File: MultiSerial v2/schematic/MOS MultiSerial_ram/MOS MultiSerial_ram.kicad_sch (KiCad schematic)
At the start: 34 parts, among them J10 ., J11 ., J12 Conn_01x01, J13 Conn_01x04, J14 Conn_01x02, J6 Conn_01x04, J7 Conn_02x04_Odd_Even, J8 ., J9 Conn_01x01, U1 6551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

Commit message: python work
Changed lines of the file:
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@@
     (effects (font (size 1.27 1.27)) (justify left bottom))
   )
-  (label "TX2" (at 14.605 46.355 0) (fields_autoplaced)
+  (label "TX2" (at 14.605 43.815 0) (fields_autoplaced)
     (effects (font (size 1.27 1.27)) (justify left bottom))
   )
@@
     (effects (font (size 1.27 1.27)) (justify right bottom))
   )
-  (label "TX3" (at 14.605 51.435 0) (fields_autoplaced)
+  (label "TX3" (at 14.605 48.895 0) (fields_autoplaced)
     (effects (font (size 1.27 1.27)) (justify left bottom))
   )
@@
     (effects (font (size 1.27 1.27)) (justify left bottom))
   )
-  (label "RX3" (at 14.605 48.895 0) (fields_autoplaced)
+  (label "RX3" (at 14.605 51.435 0) (fields_autoplaced)
     (effects (font (size 1.27 1.27)) (justify left bottom))
   )
@@
     (effects (font (size 1.27 1.27)) (justify left bottom))
   )
-  (label "RX2" (at 14.605 43.815 0) (fields_autoplaced)
-    (effects (font (size 1.27 1.27)) (justify left bottom))
-  )
+  (label "RX2" (at 14.605 46.355 0) (fields_autoplaced)
+    (effects (font (size 1.27 1.27)) (justify left bottom))
+  )

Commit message: python work
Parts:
- added J24: Conn_01x01, Connector_PinHeader_2.00mm:PinHeader_1x01_P2.00mm_Vertical, symbol Connector_Generic:Conn_01x01
- added U10: 74AHC1G08, Package_TO_SOT_SMD:SOT-23-5_HandSoldering, symbol 74xGxx:74AHC1G08
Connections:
- net +3V3: now also U10.5 (VCC)
- net GND: now also U10.3 (GND)
- net ~{CS_ACIA2}: now also J24.1 (Pin_1), U10.2
- net ~{CS_ACIA}: now also U10.1
- new net Bus/~{DOE}: U10.4
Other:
- moved on the sheet: C5, J10, J11, J12, J14, J8, J9, JP4, JP5, R1, R2, R3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

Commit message: Documentation update
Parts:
- added U11: 74AHC1G14, Package_TO_SOT_SMD:SOT-23-5, symbol 74xGxx:74AHC1G14
- added U12: 74AHC1G32, symbol 74xGxx:74AHC1G32
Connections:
- net +3V3: now also U11.5 (VCC), U12.5 (VCC)
- net Bus/~{DOE}: now also U12.4; no longer U10.4
- net GND: now also U11.3 (GND), U12.3 (GND)
- net ~{RST}: now also U11.2
- new net: U10.4, U12.1
- new net: U11.4, U12.2
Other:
- note added: "Low if CS is low and ~{RST} is high."
- note added: "Low if one or the other is low."
- moved on the sheet: J10, J11, J12, J14, J6, J7, J9, JP1, JP2, JP3, JP4, JP5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

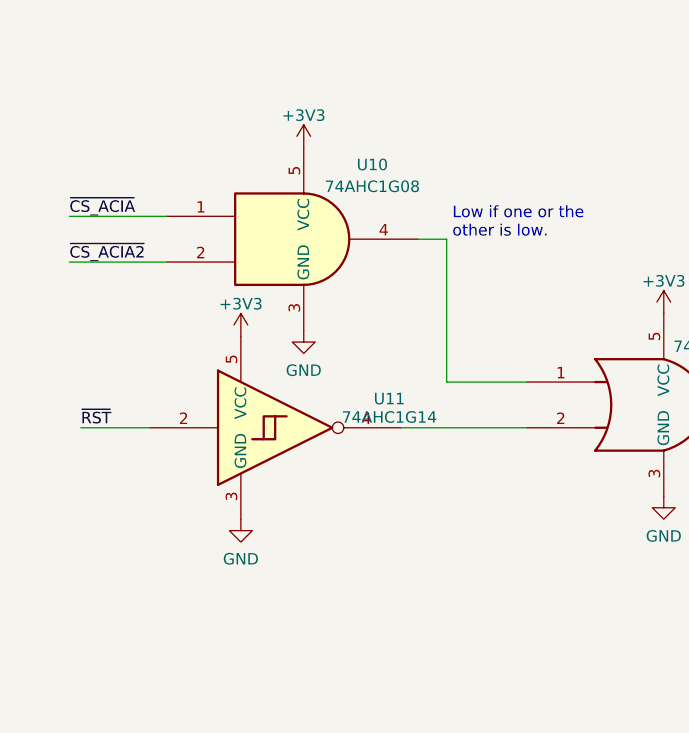
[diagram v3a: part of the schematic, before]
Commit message: Documentation update, 6800 working, new computers added
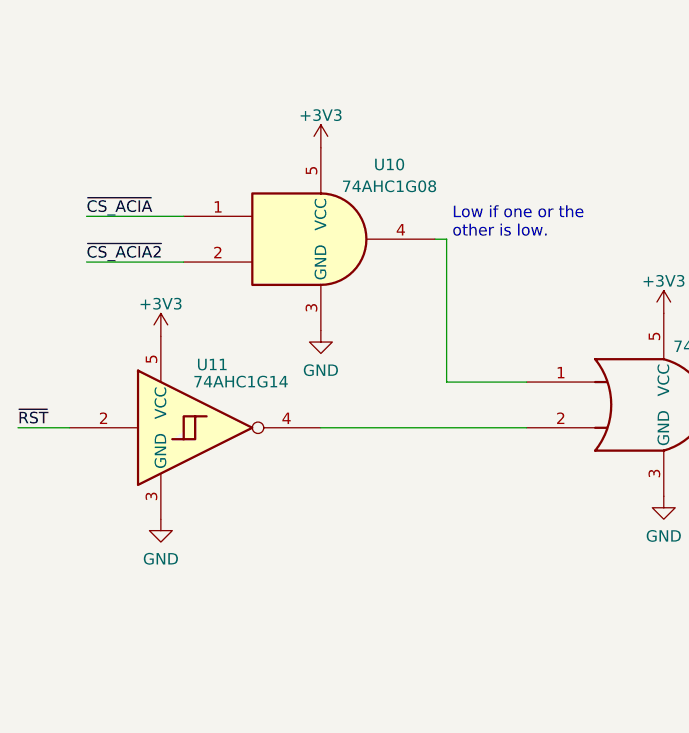
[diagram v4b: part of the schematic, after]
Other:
- moved on the sheet: U10, U11
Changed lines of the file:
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@@
     (stroke (width 0) (type default))
   )
-  (wire (pts (xy 60.96 41.91) (xy 57.785 41.91))
+  (wire (pts (xy 60.96 41.91) (xy 59.69 41.91))
     (stroke (width 0) (type default))
   )
@@
     (stroke (width 0) (type default))
   )
-  (wire (pts (xy 19.05 39.37) (xy 29.845 39.37))
+  (wire (pts (xy 20.955 39.37) (xy 31.75 39.37))
     (stroke (width 0) (type default))
   )
@@
     (stroke (width 0) (type default))
   )
-  (wire (pts (xy 69.85 62.865) (xy 55.88 62.865))
+  (wire (pts (xy 69.85 62.865) (xy 46.99 62.865))
     (stroke (width 0) (type default))
   )
@@
     (stroke (width 0) (type default))
   )
-  (wire (pts (xy 19.05 44.45) (xy 29.845 44.45))
+  (wire (pts (xy 20.955 44.45) (xy 31.75 44.45))
     (stroke (width 0) (type default))
   )
@@
     (stroke (width 0) (type default))
   )
-  (wire (pts (xy 20.32 62.865) (xy 27.94 62.865))
+  (wire (pts (xy 13.335 62.865) (xy 19.05 62.865))
     (stroke (width 0) (type default))
   )
@@
     (effects (font (size 1.27 1.27)) (justify right bottom))
   )
-  (label "~{CS_ACIA}" (at 19.05 39.37 0) (fields_autoplaced)
+  (label "~{CS_ACIA}" (at 20.955 39.37 0) (fields_autoplaced)
     (effects (font (size 1.27 1.27)) (justify left bottom))
   )
@@
     (effects (font (size 1.27 1.27)) (justify left bottom))
   )
-  (label "~{CS_ACIA2}" (at 19.05 44.45 0) (fields_autoplaced)
+  (label "~{CS_ACIA2}" (at 20.955 44.45 0) (fields_autoplaced)
     (effects (font (size 1.27 1.27)) (justify left bottom))
   )
@@
     (effects (font (size 1.27 1.27)) (justify left bottom))
   )
-  (label "~{RST}" (at 20.32 62.865 0) (fields_autoplaced)
+  (label "~{RST}" (at 13.335 62.865 0) (fields_autoplaced)
     (effects (font (size 1.27 1.27)) (justify left bottom))
   )
@@
     )
   )
-  (symbol (lib_id "power:+3V3") (at 38.1 52.705 0) (unit 1)
+  (symbol (lib_id "power:+3V3") (at 29.21 52.705 0) (unit 1)
     (in_bom yes) (on_board yes) (dnp no) (fields_autoplaced)
-    (property "Reference" "#PWR062" (at 38.1 56.515 0)
+    (property "Reference" "#PWR062" (at 29.21 56.515 0)
       (effects (font (size 1.27 1.27)) hide)
     )
-    (property "Value" "+3V3" (at 38.1 49.1292 0)
+    (property "Value" "+3V3" (at 29.21 49.1292 0)
       (effects (font (size 1.27 1.27)))
     )
-    (property "Footprint" "" (at 38.1 52.705 0)
+    (property "Footprint" "" (at 29.21 52.705 0)
       (effects (font (size 1.27 1.27)) hide)
     )
-    (property "Datasheet" "" (at 38.1 52.705 0)
+    (property "Datasheet" "" (at 29.21 52.705 0)
       (effects (font (size 1.27 1.27)) hide)
     )
@@
     )
   )
-  (symbol (lib_id "power:GND") (at 38.1 73.025 0) (unit 1)
+  (symbol (lib_id "power:GND") (at 29.21 73.025 0) (unit 1)
     (in_bom yes) (on_board yes) (dnp no) (fields_autoplaced)
-    (property "Reference" "#PWR063" (at 38.1 79.375 0)
+    (property "Reference" "#PWR063" (at 29.21 79.375 0)
       (effects (font (size 1.27 1.27)) hide)
     )
-    (property "Value" "GND" (at 38.1 77.4684 0)
+    (property "Value" "GND" (at 29.21 77.4684 0)
       (effects (font (size 1.27 1.27)))
     )
-    (property "Footprint" "" (at 38.1 73.025 0)
+    (property "Footprint" "" (at 29.21 73.025 0)
       (effects (font (size 1.27 1.27)) hide)
     )
-    (property "Datasheet" "" (at 38.1 73.025 0)
+    (property "Datasheet" "" (at 29.21 73.025 0)
       (effects (font (size 1.27 1.27)) hide)
     )
@@
     )
   )
-  (symbol (lib_id "power:GND") (at 45.085 52.07 0) (unit 1)
+  (symbol (lib_id "power:GND") (at 46.99 52.07 0) (unit 1)
     (in_bom yes) (on_board yes) (dnp no) (fields_autoplaced)
-    (property "Reference" "#PWR061" (at 45.085 58.42 0)
+    (property "Reference" "#PWR061" (at 46.99 58.42 0)
       (effects (font (size 1.27 1.27)) hide)
     )
-    (property "Value" "GND" (at 45.085 56.5134 0)
+    (property "Value" "GND" (at 46.99 56.5134 0)
       (effects (font (size 1.27 1.27)))
     )
-    (property "Footprint" "" (at 45.085 52.07 0)
+    (property "Footprint" "" (at 46.99 52.07 0)
       (effects (font (size 1.27 1.27)) hide)
     )
-    (property "Datasheet" "" (at 45.085 52.07 0)
+    (property "Datasheet" "" (at 46.99 52.07 0)
       (effects (font (size 1.27 1.27)) hide)
     )
@@
     )
   )
-  (symbol (lib_id "power:+3V3") (at 45.085 31.75 0) (unit 1)
+  (symbol (lib_id "power:+3V3") (at 46.99 31.75 0) (unit 1)
     (in_bom yes) (on_board yes) (dnp no) (fields_autoplaced)
-    (property "Reference" "#PWR060" (at 45.085 35.56 0)
+    (property "Reference" "#PWR060" (at 46.99 35.56 0)
       (effects (font (size 1.27 1.27)) hide)
     )
-    (property "Value" "+3V3" (at 45.085 28.1742 0)
+    (property "Value" "+3V3" (at 46.99 28.1742 0)
       (effects (font (size 1.27 1.27)))
     )
-    (property "Footprint" "" (at 45.085 31.75 0)
+    (property "Footprint" "" (at 46.99 31.75 0)
       (effects (font (size 1.27 1.27)) hide)
     )
-    (property "Datasheet" "" (at 45.085 31.75 0)
+    (property "Datasheet" "" (at 46.99 31.75 0)
       (effects (font (size 1.27 1.27)) hide)
     )
@@
     )
   )
-  (symbol (lib_id "74xGxx:74AHC1G14") (at 43.18 62.865 0) (unit 1)
-    (in_bom yes) (on_board yes) (dnp no) (fields_autoplaced)
-    (property "Reference" "U11" (at 54.5968 59.6661 0)
+  (symbol (lib_id "74xGxx:74AHC1G14") (at 34.29 62.865 0) (unit 1)
+    (in_bom yes) (on_board yes) (dnp no)
+    (property "Reference" "U11" (at 34.925 55.88 0)
       (effects (font (size 1.27 1.27)))
     )
-    (property "Value" "74AHC1G14" (at 54.5968 61.7141 0)
+    (property "Value" "74AHC1G14" (at 38.1 57.785 0)
       (effects (font (size 1.27 1.27)))
     )
-    (property "Footprint" "Package_TO_SOT_SMD:SOT-23-5" (at 43.18 62.865 0)
+    (property "Footprint" "Package_TO_SOT_SMD:SOT-23-5" (at 34.29 62.865 0)
       (effects (font (size 1.27 1.27)) hide)
     )
-    (property "Datasheet" "https://www.ti.com/lit/ds/symlink/sn74lvc1g14.pdf" (at 43.18 62.865 0)
+    (property "Datasheet" "https://www.ti.com/lit/ds/symlink/sn74lvc1g14.pdf" (at 34.29 62.865 0)
       (effects (font (size 1.27 1.27)) hide)
     )
@@
     )
   )
-  (symbol (lib_id "74xGxx:74AHC1G08") (at 45.085 41.91 0) (unit 1)
+  (symbol (lib_id "74xGxx:74AHC1G08") (at 46.99 41.91 0) (unit 1)
     (in_bom yes) (on_board yes) (dnp no)
-    (property "Reference" "U10" (at 52.705 33.655 0)
+    (property "Reference" "U10" (at 54.61 33.655 0)
       (effects (font (size 1.27 1.27)))
     )
-    (property "Value" "74AHC1G08" (at 52.705 36.0792 0)
+    (property "Value" "74AHC1G08" (at 54.61 36.0792 0)
       (effects (font (size 1.27 1.27)))
     )
-    (property "Footprint" "Package_TO_SOT_SMD:SOT-23-5_HandSoldering" (at 45.085 41.91 0)
+    (property "Footprint" "Package_TO_SOT_SMD:SOT-23-5_HandSoldering" (at 46.99 41.91 0)
       (effects (font (size 1.27 1.27)) hide)
     )
-    (property "Datasheet" "http://www.ti.com/lit/sg/scyt129e/scyt129e.pdf" (at 45.085 41.91 0)
+    (property "Datasheet" "http://www.ti.com/lit/sg/scyt129e/scyt129e.pdf" (at 46.99 41.91 0)
       (effects (font (size 1.27 1.27)) hide)
     )
